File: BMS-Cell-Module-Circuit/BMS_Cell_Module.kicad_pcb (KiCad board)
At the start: 2 copper layers, 45.7 x 65.8 mm, 35 parts, among them J1 Conn_01x02_Female, J2 Conn_01x04_Female, J3 Conn_01x04_Female, M1 SI2312BDS-T1-E3, U2 ADUM1250ARZ, U3 ATTINY85V-10SU 8S2 EIAJ SOIC

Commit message: First check in
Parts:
- removed the J3 at (173.1, 67.3)
- removed M1: SI2312BDS-T1-E3, TO_SOT_Packages_SMD:SOT-23
- removed R11: REG710NA-3.3, TO_SOT_Packages_SMD:SOT-23-6_Handsoldering
- removed the REF** at (174.3, 123.4)
- removed the REF** at (134.0, 123.4)
- removed the REF** at (133.9, 63.0)
- added J2: Conn_01x04_Female, Connectors_JST:JST_PH_S4B-PH-K_04x2.00mm_Angled, F.Cu at (152.3, 92.3)
- added Q1: SI2312BDS-T1-E3, Package_TO_SOT_SMD:SOT-23, F.Cu at (171.6, 79.7)
- added REF**: PinHeader_1x04_P2.54mm_NoSilk, ATTINY:PinHeader_1x04_P2.54mm_NoSilk, F.Cu at (164.3, 90.5)
- added REF**: 2.7mm M2.5, MountingHole:MountingHole_2.7mm_M2.5, F.Cu at (110.8, 96.6)
- added REF**: OSHW-Logo2_7.3x6mm_SilkScreen, Symbol:OSHW-Logo2_7.3x6mm_SilkScreen, F.Cu at (125.7, 74.3)
- added REF**: PinHeader_1x04_P2.54mm_NoSilk, ATTINY:PinHeader_1x04_P2.54mm_NoSilk, F.Cu at (151.5, 90.5)
- added REF**: PinHeader_1x02_P2.54mm_NoSilk, ATTINY:PinHeader_1x02_P2.54mm_NoSilk, F.Cu at (119.8, 90.5)
- added TP2: TPGND, TestPoint:TestPoint_Pad_D1.5mm, F.Cu at (120.9, 73.2)
- added U1: REG710NA-3.3, TO_SOT_Packages_SMD:SOT-23-6_Handsoldering, F.Cu at (134.6, 96.4)
- C1, C2: value 2.2uF Ceramic X7R -> 2.2uF; footprint Capacitors_SMD:C_1206_HandSoldering -> Capacitor_SMD:C_0805_2012Metric_Pad1.33x1.40mm_HandSolder
- C3, C4, C5: footprint Capacitors_SMD:C_1206_HandSoldering -> Capacitor_SMD:C_0805_2012Metric_Pad1.33x1.40mm_HandSolder
- C6: value 0.22uF Ceramic X7R -> 0.22uF; footprint Capacitors_SMD:C_1206_HandSoldering -> Capacitor_SMD:C_0805_2012Metric_Pad1.33x1.40mm_HandSolder
- D1: value SE30AFG-M3/6A -> SS34 Schottky 40V/3A
- D2, D4: footprint LEDs:LED_1206_HandSoldering -> LED_SMD:LED_0805_2012Metric_Pad1.15x1.40mm_HandSolder
- F1: value MC36228 1.5A 8V -> FUSE; footprint Resistors_SMD:R_1812_HandSoldering -> Resistor_SMD:R_1812_4532Metric_Pad1.42x3.40mm_HandSolder
- R1: value HS50 3R3 J 50W Axial Wire Wound -> 2R/10W; footprint Resistors_THT:R_Axial_Power_L50.0mm_W9.0mm_P60.96mm -> ATTINY:R_Axial_Power_L48.0mm_W9.5mm_P60.96mm
- R10, R12, R4, R5, R6, R7, R8, R9: footprint Resistors_SMD:R_1206_HandSoldering -> Resistor_SMD:R_0805_2012Metric_Pad1.33x1.40mm_HandSolder
- R2: value 47R -> 2K; footprint Resistors_SMD:R_1206_HandSoldering -> Resistor_SMD:R_0805_2012Metric_Pad1.33x1.40mm_HandSolder
- R3: value 20K -> 68K; footprint Resistors_SMD:R_1206_HandSoldering -> Resistor_SMD:R_0805_2012Metric_Pad1.33x1.40mm_HandSolder
- REF**: value 1pin -> 2.7mm M2.5; footprint Connectors:1pin -> MountingHole:MountingHole_2.7mm_M2.5
- TP1: footprint Connectors:PINTST -> TestPoint:TestPoint_Pad_D1.5mm
- U2: footprint adum1250:ADUM1250 -> Package_SO:SOIC-8_3.9x4.9mm_P1.27mm
- U3: footprint ATTINY:ATTINY85V -> Package_SO:SOIJ-8_5.3x5.3mm_P1.27mm
- moved R7 66.6 mm to (110.0, 74.8), turned to 90 degrees
- moved R6 61.9 mm to (112.5, 74.8), turned to 270 degrees
- moved R5 55.0 mm to (115.0, 74.8), turned to 90 degrees
- moved C3 49.8 mm to (111.2, 78.2), turned to 0 degrees
- moved J1 48.7 mm to (120.1, 92.3)
- moved TP1 45.3 mm to (120.8, 75.7), turned to 180 degrees
- moved C1 44.7 mm to (129.7, 97.0), turned to 180 degrees
- moved C6 42.6 mm to (129.7, 94.5), turned to 0 degrees
- moved R12 40.3 mm to (135.6, 74.8), turned to 270 degrees
- moved C2 37.5 mm to (129.7, 92.0), turned to 180 degrees
- moved R1 34.1 mm to (171.6, 83.2), turned to 180 degrees
- moved C5 33.6 mm to (139.8, 92.0), turned to 180 degrees
- moved D4 33.2 mm to (138.1, 74.8), turned to 270 degrees
- moved R9 29.0 mm to (168.3, 79.7), turned to 90 degrees
- moved ISP1 27.6 mm to (142.4, 75.2)
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- renumbered J2 to J3
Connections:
- J1 pad 1: BATT+RAW -> GND
- J1 pad 2: GND -> BATT+RAW
- R10 pad 1: /SDA -> /SCK
- R8 pad 1: 3V3 -> /SDA
- R8 pad 2: /SCK -> 3V3
- U2 pad 1: Net-(J2-Pad1) -> 3V3
- U2 pad 2: Net-(J2-Pad2) -> /SDA
- U2 pad 3: Net-(J2-Pad3) -> /SCK
- U2 pad 4: Net-(J2-Pad4) -> GND
- U2 pad 5: GND -> Net-(J2-Pad4)
- U2 pad 6: /SCK -> Net-(J2-Pad3)
- U2 pad 7: /SDA -> Net-(J2-Pad2)
- U2 pad 8: 3V3 -> Net-(J2-Pad1)
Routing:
- net GND: track 164.5 -> 10.9 mm, vias 3 -> 39
- net Net-(C1-Pad1): track 93.3 -> 54.2 mm, vias 3 -> 0
- net Net-(C3-Pad1): track 21.1 -> 48.9 mm, vias 0 -> 2
- net /PB4BYPASS: track 17.6 -> 43.1 mm
- net Net-(J2-Pad2): track 18.9 -> 38.7 mm
- net BATT+RAW: track 49.6 -> 30.3 mm, vias 2 -> 1
- net Net-(J2-Pad3): track 19.5 -> 37.9 mm
- net Net-(J2-Pad1): track 18.7 -> 36.6 mm
- net 3V3: track 95.1 -> 79.2 mm, vias 3 -> 1
- net Net-(Q1-Pad3): track 61.6 -> 46.0 mm, vias 2 -> 1
- net Net-(J2-Pad4): track 20.7 -> 36.2 mm
- net /SDA: track 46.1 -> 36.8 mm, vias 4 -> 3
- net Net-(C6-Pad1): track 3.50 -> 10.3 mm
- net /SCK: track 41.2 -> 35.2 mm, vias 3 -> 2
- net Net-(D4-Pad1): track 6.63 -> 2.54 mm
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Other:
- board size 45.7 x 65.8 mm -> 65 x 28 mm
- net class Default: trace_width 0.35 -> 0.25; via_dia 0.6 -> 0.65; via_drill 0.4 -> 0.3
- net class Power added: clearance 0.3, trace_width 1, via_dia 2, via_drill 0.8
- net class PowerAT added: clearance 0.3, trace_width 0.35, via_dia 0.65, via_drill 0.3
- rule trace_min: 0.35 -> 0.25
- board text added: "+"
- board text added: "-"
- board text added: "1.8→4.35V/2A"
- board text added: "ATTINY85 PROGRAM"
- board text added: "BATT"
- board text added: "FUSE"
- board text added: "I2C IN"
- board text added: "I2C OUT"
- board text added: "M2.5"
- board text added: "SCL"
- board text added: "SDA"
- board text added: "TH1"
- board text added: "V3.0 (Sep 2018)"
- board text added: "diyBMS"
- board text added: "github.com/stuartpittaway/diyBMS Redesigned PCB by Nick Smith © 2017 Stuart Pittaway"
- board text added: "github.com/stuartpittaway/diyBMS © 2017 Stuart Pittaway"
- board text removed: "(c)2017 Stuart Pittaway"
- board text removed: "(c)2017 Stuart Pittaway #MadeInTheBlackCountry"
- board text removed: "BATT+"
- board text removed: "DIYBMS"
- board text removed: "GND"
- board text removed: "PIN 1"
- board text removed: "Version 2.1 (Mar 2018)"
- board text removed: "https://github.com/stuartpittaway/diyBMS"

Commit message: Updated images
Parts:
- R10, R12, R8: value 2K2 -> 4K7
- R2: value 2K -> 4K7
- R3: value 68K -> 20K
- R6: value 470K -> 510K
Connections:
- net /RESET renamed /RST
- net /SDA renamed /MOSI
- R6 pad 1: Net-(R5-Pad2) -> BATT+RAW

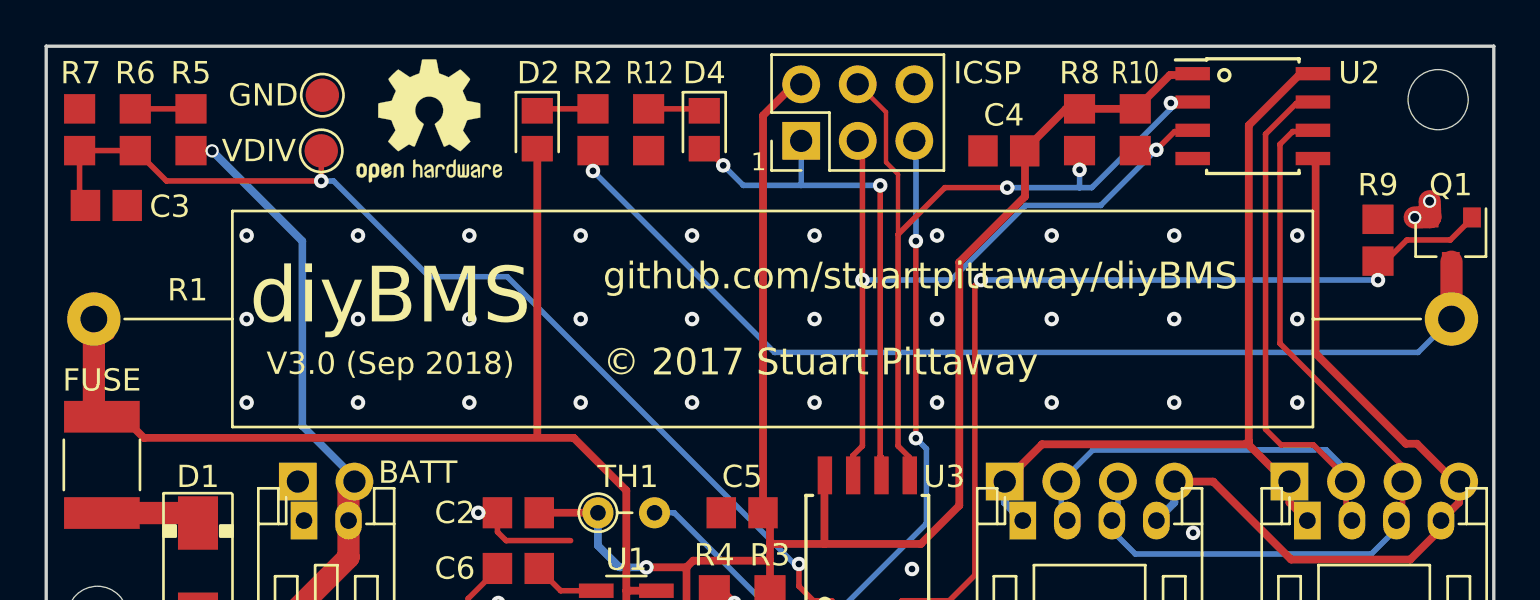
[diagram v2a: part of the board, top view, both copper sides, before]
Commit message: Removed URLs for incorrect sized compontents
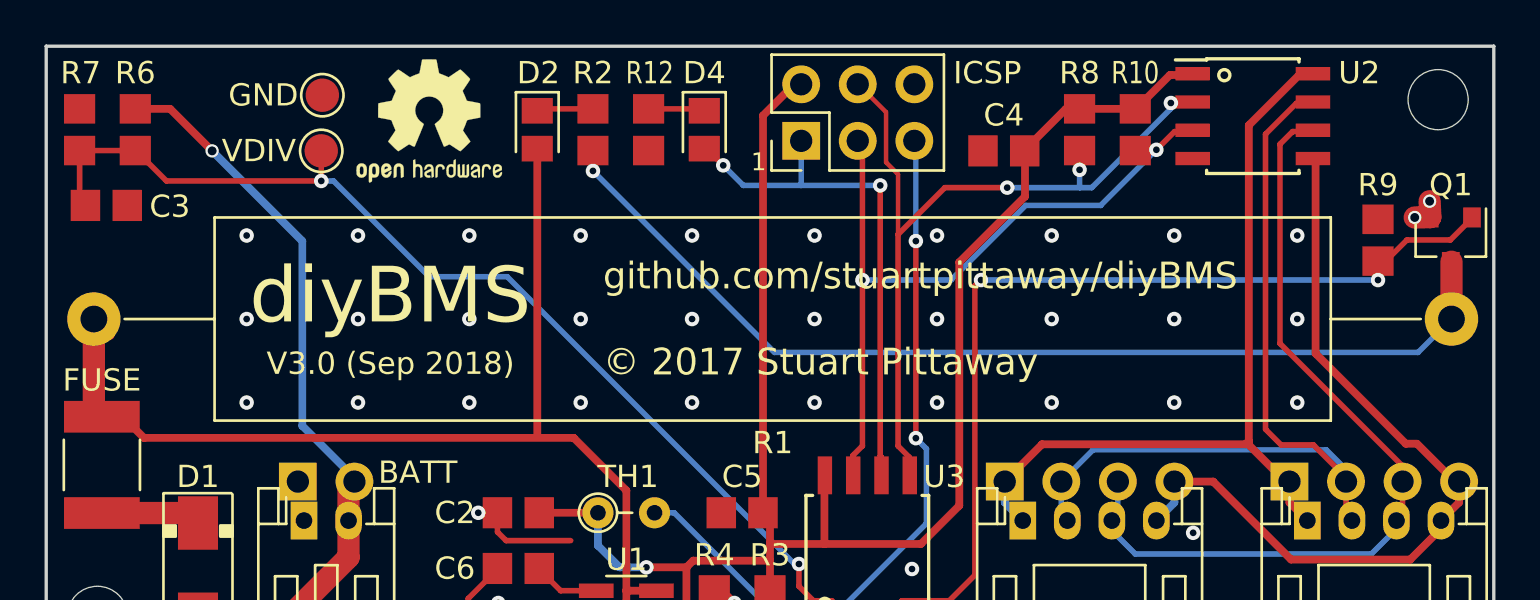
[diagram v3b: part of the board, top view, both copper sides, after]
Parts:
- removed R5: 47K, Resistor_SMD:R_0805_2012Metric_Pad1.33x1.40mm_HandSolder
- R1: footprint ATTINY:R_Axial_Power_L48.0mm_W9.5mm_P60.96mm -> Resistors_THT:R_Axial_Power_L50.0mm_W9.0mm_P60.96mm
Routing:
- net BATT+RAW: track 30.3 -> 33.6 mm
- net Net-(R5-Pad2): track 2.50 -> 0.00 mm

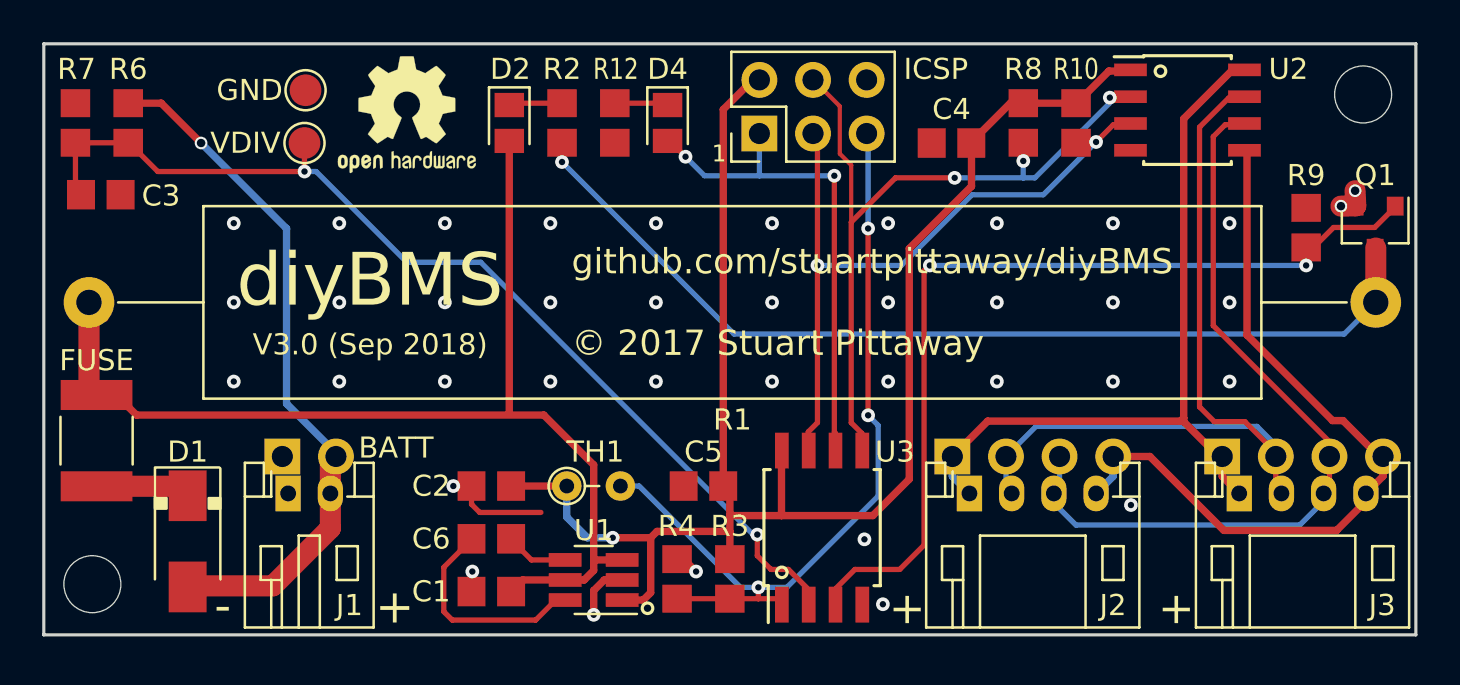
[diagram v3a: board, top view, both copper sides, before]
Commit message: Updated Gerber files after removal of R5
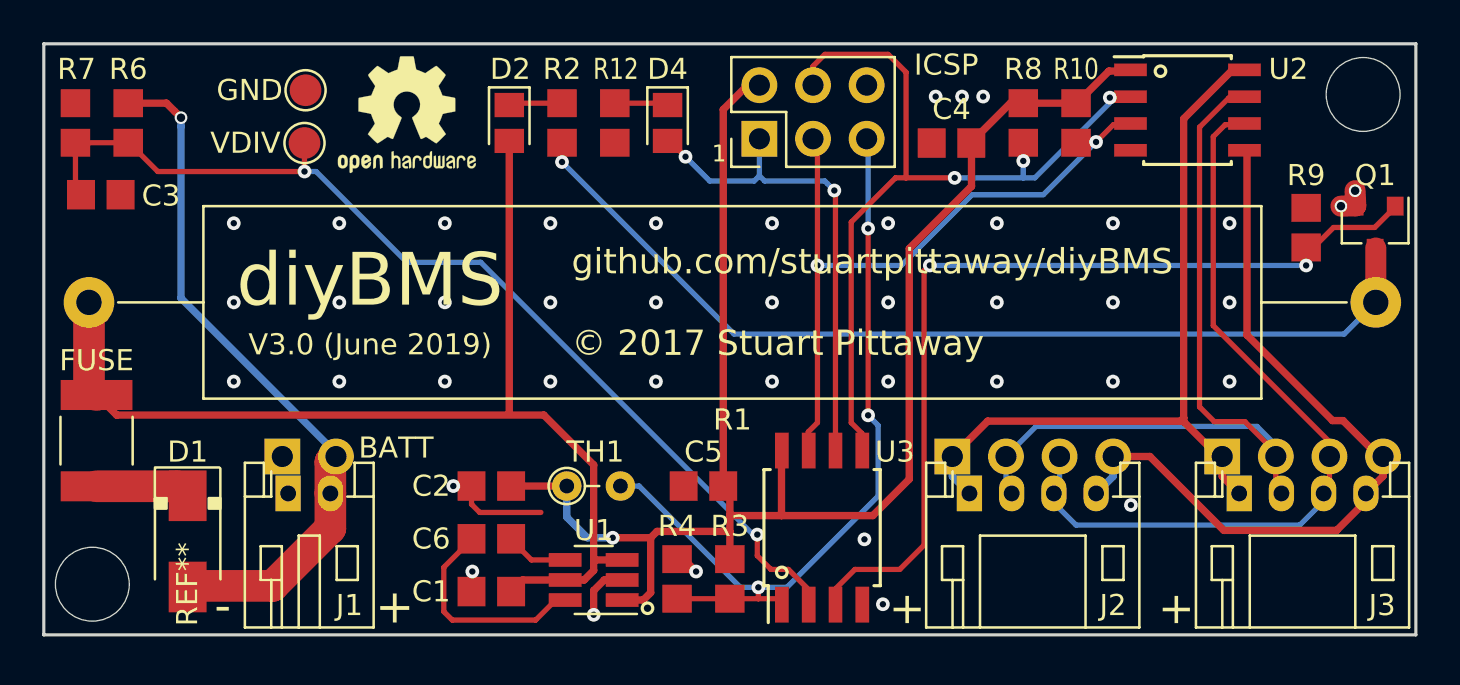
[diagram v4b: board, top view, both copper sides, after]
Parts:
- REF** (x2): value 2.7mm M2.5 -> 3.5mm; footprint MountingHole:MountingHole_2.7mm_M2.5 -> Mounting_Holes:MountingHole_3.5mm
- moved ISP1 0.25 mm to (142.4, 75.5)
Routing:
- net /MOSI: track 36.8 -> 39.7 mm
- net /SCK: track 35.2 -> 34.6 mm
- net GND: track 10.9 -> 10.8 mm, vias 39 -> 42
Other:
- board text added: "V3.0 (June 2019)"
- board text added: "github.com/stuartpittaway/diyBMS Redesigned PCB by Nick Smith © 2017-19 Stuart Pittaway"
- board text removed: "M2.5"
- board text removed: "V3.0 (Sep 2018)"
- board text removed: "github.com/stuartpittaway/diyBMS Redesigned PCB by Nick Smith © 2017 Stuart Pittaway"
